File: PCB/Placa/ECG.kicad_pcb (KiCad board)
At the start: 2 copper layers, 40.6 x 23 mm, 32 parts, among them P1 RA, P2 LL, P3 RL, P4 OUT, P5 5V, P6 GND, P7 Shield, P8 Out_ina, U1 INA333, U2 OPA2335, U3 OPA2335, U4 REF5050, U5 REF3125

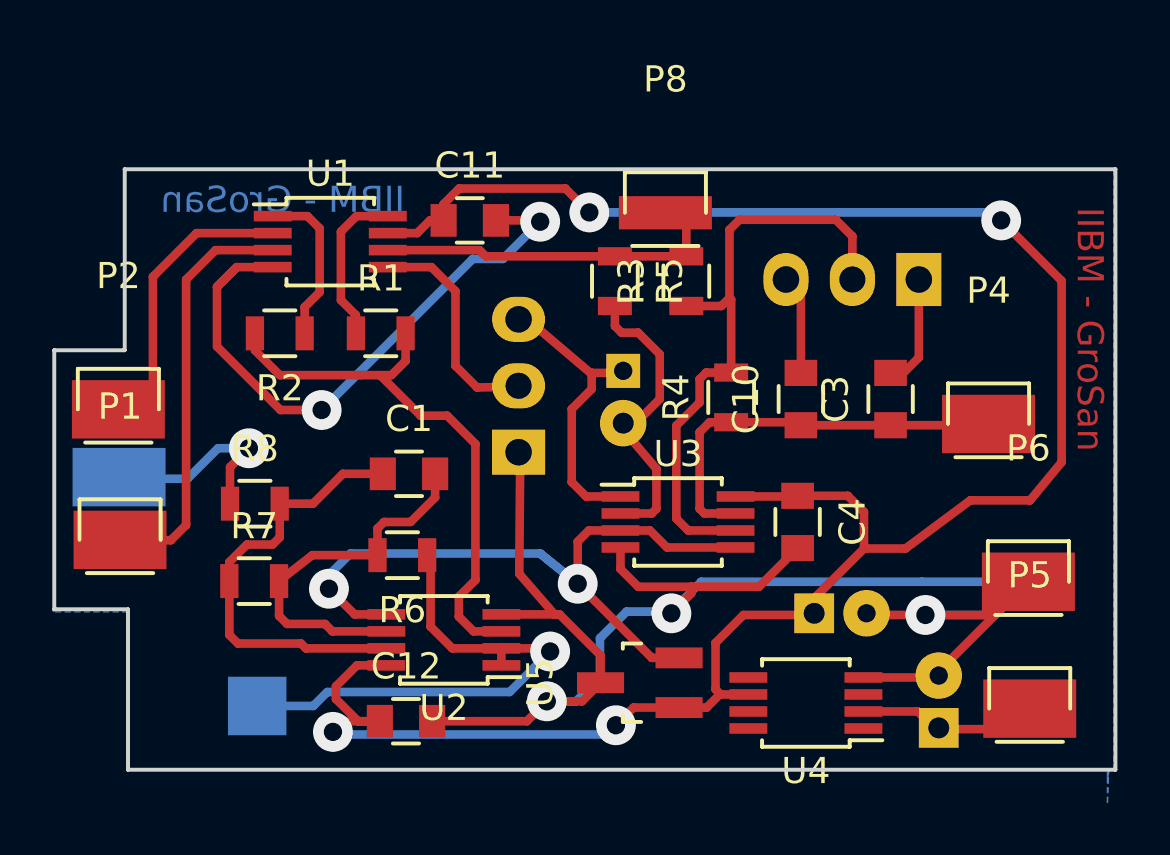
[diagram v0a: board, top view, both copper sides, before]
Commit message: PCB
- Cambios del circuito. Actualizado a la versión final del prototipo en
cajita 19/11.
- Algunos cambios en pistas.
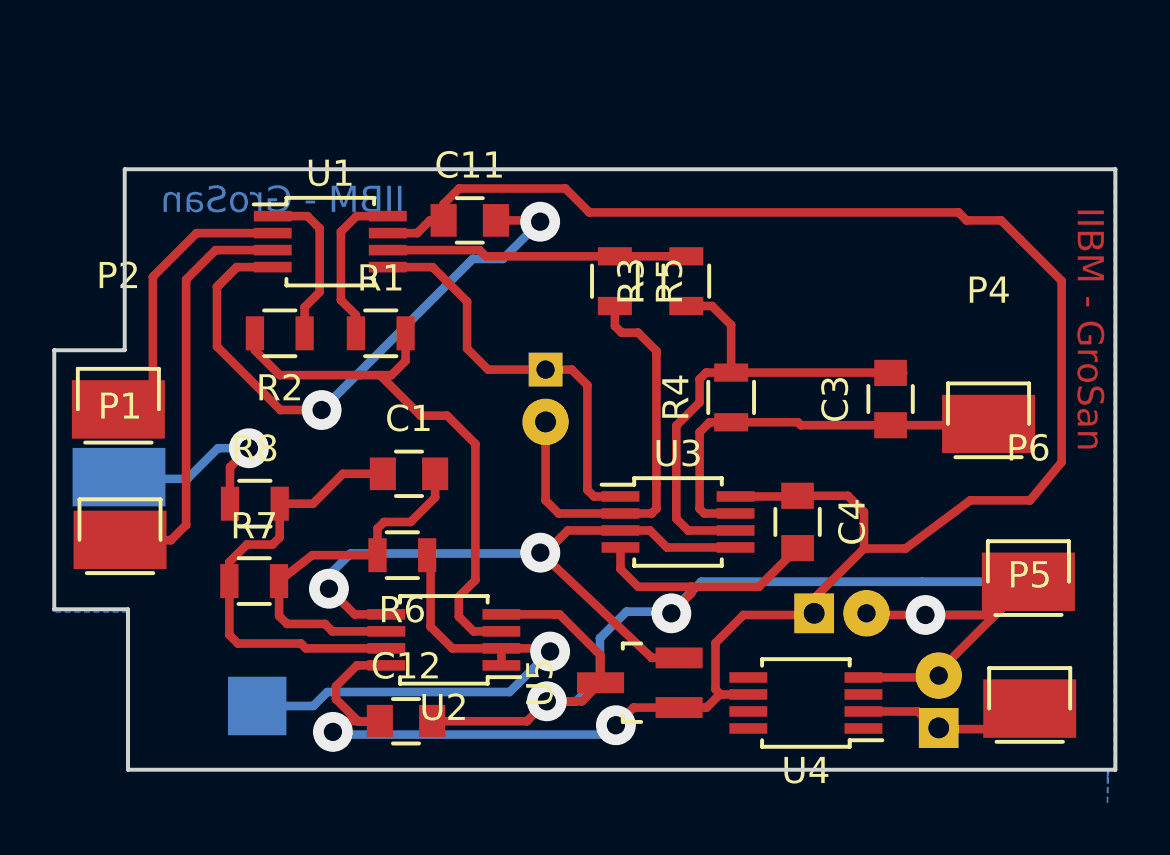
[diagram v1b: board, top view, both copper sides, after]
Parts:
- removed C10: 100n, Capacitors_SMD:C_0805
- removed JP1: GND/AC, Pin_Headers:Pin_Header_Straight_1x03
- removed JP2: C3/C10, Pin_Headers:Pin_Header_Straight_1x03
- removed P8: Out_ina, Pin_Headers:Pin_Header_Straight_1x01
- C1: value 47p -> 10n
- C3: value 330p -> 330n
- R1, R2: value 12.7k -> 12k
- R3: value 4.7k -> 100
- R4: value 10.7k -> 10k
- R5: value 316k -> 330k
- R7: value 390k -> 2.2k
- U5: value REF3125 -> REF3112
- moved C2 2.97 mm to (130.0, 75.2)
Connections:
- net INA renamed Net-(R3-Pad2)
- R3 pad 1: Net-(JP2-Pad2) -> Net-(C3-Pad2)
- R4 pad 2: Net-(JP2-Pad2) -> Net-(C3-Pad2)
- U1 pad 5: Net-(JP1-Pad2) -> Net-(C2-Pad1)
- U3 pad 6: Net-(JP2-Pad2) -> Net-(C3-Pad2)
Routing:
- net Net-(JP2-Pad2): track 23.7 -> 0.00 mm
- net Net-(C3-Pad2): track 4.31 -> 20.1 mm
- net Net-(JP1-Pad2): track 8.64 -> 0.00 mm
- net GND: track 94.1 -> 87.5 mm
- net Net-(C2-Pad1): track 10.9 -> 15.9 mm
- net Net-(C10-Pad2): track 4.54 -> 0.00 mm
- net Net-(C2-Pad2): track 12.3 -> 16.3 mm
- net REF: track 28.4 -> 26.6 mm
- net Net-(R3-Pad2): track 13.4 -> 11.8 mm
- net +5V: vias 4 -> 2
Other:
- net class Default: clearance 0.3048 -> 0.1778
- rule trace_clearance: 0.3048 -> 0.1778
